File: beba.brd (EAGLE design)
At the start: 35 x 56 mm, 56 parts, among them IC202 LM74670QDGKTQ1, IC302 LM74670QDGKTQ1, IC402 LM74670QDGKTQ1, IC507 579-MCP73871T2CCIML, IC601 TPS630701RNMT, Q202 SQ2310ES-T1_BE3, Q302 SQ2310ES-T1_BE3, Q402 SQ2310ES-T1_BE3

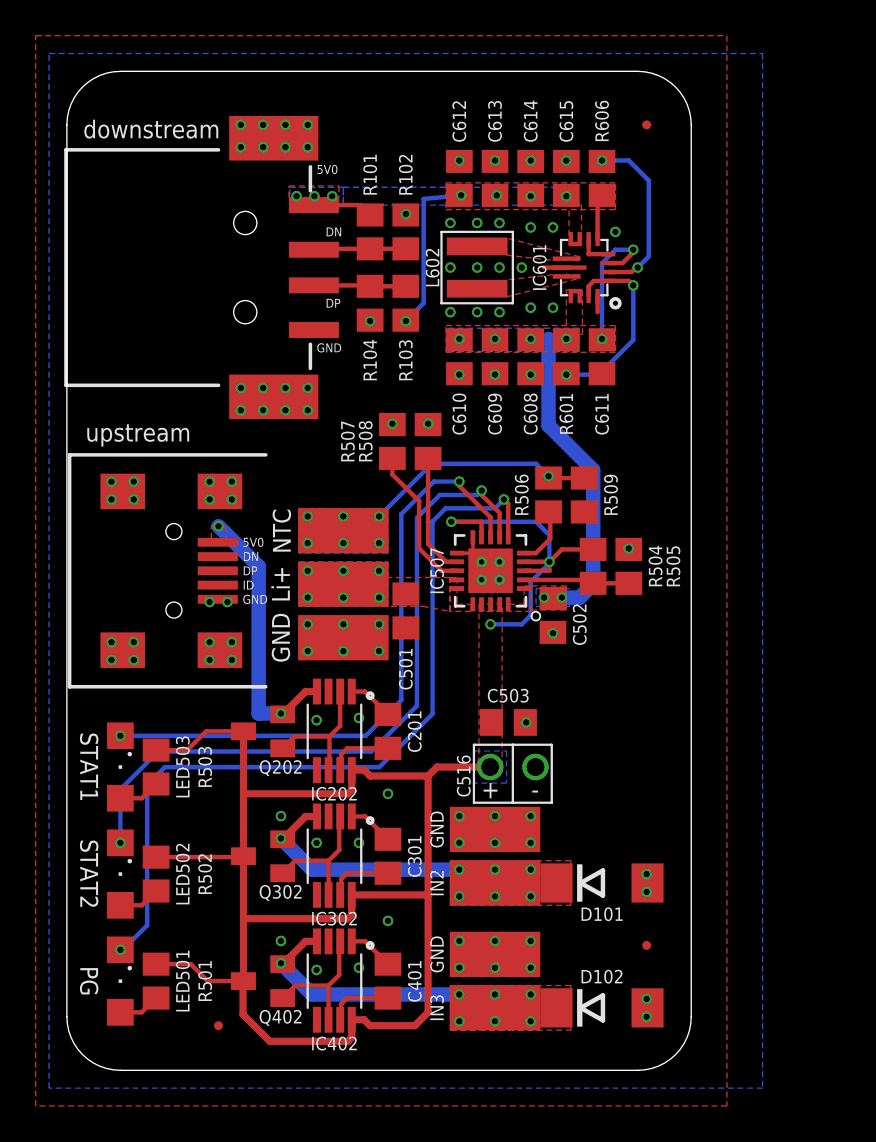
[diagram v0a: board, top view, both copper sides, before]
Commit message: start of rev.2 board - increased uninterrupted copper below MCP73871 for better cooling - removed bottom copper contacts for IN1/IN2, GND and similar - replaced MCP73871's big input cap from TH to SMD - replaced NTC solderpads with 0805 component
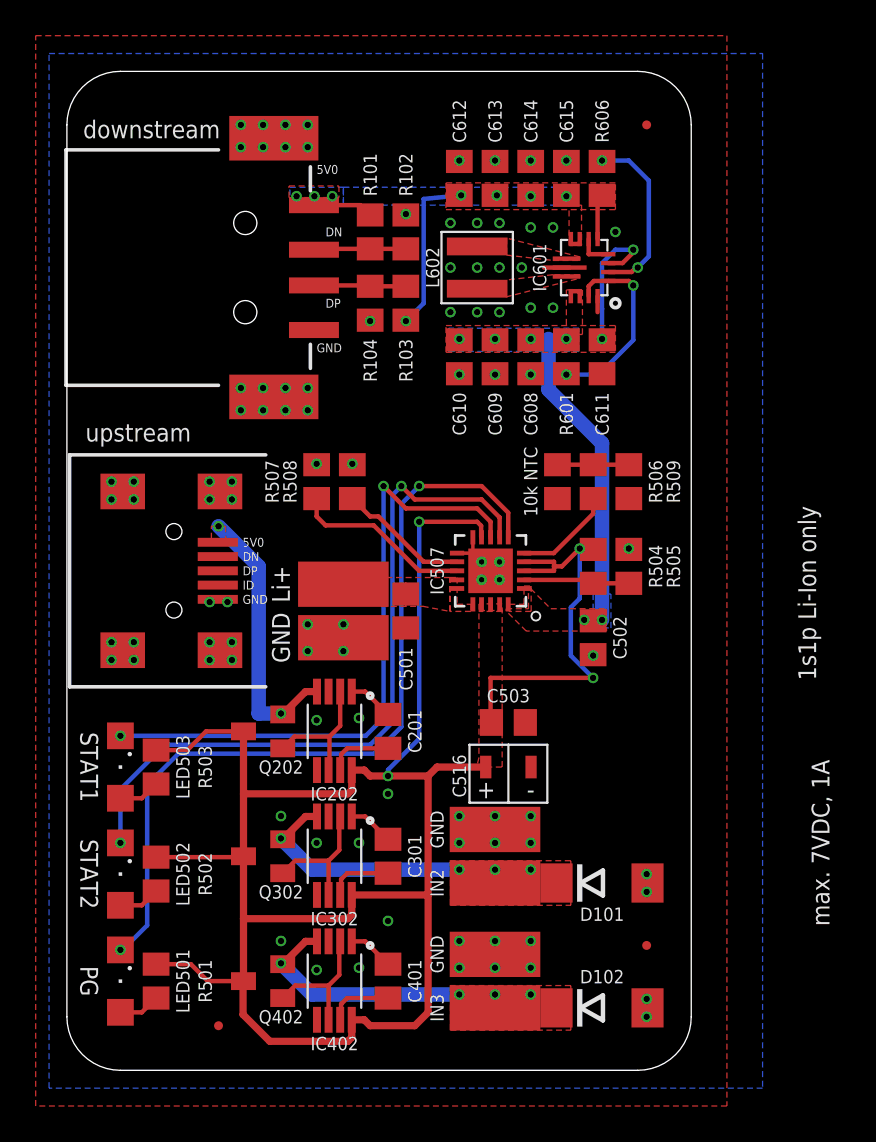
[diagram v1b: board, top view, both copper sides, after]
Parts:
- removed PAD105: NTC, wirepad:SMD2,54-5,08
- added R1: 10k NTC, beta 3892, rcl:R0805
- C516: device C-Pol:TH -> C-Pol:SMD
- moved R507 4.81 mm to (-44.0, 158.0)
- moved R508 4.81 mm to (-42.0, 158.0)
- moved R506 2.61 mm to (-28.5, 158.0)
- moved R509 2.61 mm to (-26.5, 158.0)
- moved C502 2.57 mm to (-28.5, 149.2)
- moved C516 0.25 mm to (-33.2, 142.0)
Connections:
- net GND: now also R1.1
- net NTC: now also R1.2; no longer PAD105.1
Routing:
- net V_INPUT: track 106.0 -> 125.8 mm, vias 3 -> 4
- net NTC: track 13.8 -> 4.00 mm, vias 7 -> 0
- net VINPUT2: track 16.3 -> 20.3 mm, vias 7 -> 4
- net VINPUT3: track 13.3 -> 17.3 mm, vias 7 -> 4
- net MCP73871-1:THERM: track 3.35 -> 5.64 mm
- net MCP73871-1:PROG1: track 8.31 -> 10.1 mm
- net MCP73871-1:PG: track 45.1 -> 46.4 mm
- net MCP73871-1:STAT2: track 39.4 -> 40.6 mm
- net MCP73871-1:STAT1: track 34.9 -> 35.9 mm
- net V_LIION+: track 0.75 -> 0.00 mm, vias 6 -> 0
- net MCP73871-1:PROG3: track 6.83 -> 7.34 mm
- net GND: vias 96 -> 93
- removed copper zone on layer 16, net NTC
- removed copper zone on layer 16, net VINPUT2
- removed copper zone on layer 16, net VINPUT3
- removed copper zone on layer 16, net V_INPUT
- removed copper zone on layer 16, net V_LIION+
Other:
- board text added: "10k NTC"
- board text removed: "NTC"

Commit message: further work on rev.2 board: - increased copper below MCP73871 even more - replaced solder pads for LiIon battery with SMD JST-PH connector
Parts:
- removed FID2: fiducial, fiducials:FIDUCIAL_0.5MM
- removed PAD106: Li-Ion +, wirepad:SMD2,54-5,08
- removed PAD107: GND, wirepad:SMD2,54-5,08
- removed R1: 10k NTC, beta 3892, rcl:R0805
- added FID102: fiducial, fiducials:FIDUCIAL_0.5MM
- added J101: S2B-PH-SM4-TB(LF)(SN), JST-PH:JST_S2B-PH-SM4-TB(LF)(SN)
- added R105: 49k9, resistor:R0805
- added SW701: (no value), JS102011SAQN SPDT slide switch:SMD
- R101: value 75k -> 10k NTC, beta 3892; device resistor:R0805 -> rcl:R0805
- R102, R104: value 49k9 -> 75k
- R103: value 75k -> 49k9
- moved R101 17.5 mm to (-30.5, 158.0)
- moved C611 10.2 mm to (-26.0, 175.0), turned to 270 degrees
- moved R507 6.26 mm to (-41.0, 163.5)
- moved R508 6.26 mm to (-39.0, 163.5)
- moved R103 4.00 mm to (-39.0, 172.0)
- moved R102 2.00 mm to (-41.0, 172.0), turned to 90 degrees
- moved R104 2.00 mm to (-39.0, 168.0), turned to 270 degrees
- moved C501 1.80 mm to (-37.5, 149.8)
- renumbered FID1 to FID101, FID3 to FID103
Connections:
- removed net TPS630701-1:N$8: IC601.1-PS/S, IC601.14-EN, R601.1
- new net TPS630701-1:EN: IC601.14-EN, SW701.C
- new net TPS630701-1:SP/S: IC601.1-PS/S, R601.1, SW701.2
- net 5V0: now also R102.2, R104.2; no longer R101.2, R103.2
- net GND: now also J101.2, J101.S1, J101.S2, R101.1, R103.1, R105.1, SW701.1; no longer PAD107.1, R1.1, R102.1, R104.1
- net NTC: now also R101.2; no longer R1.2
- net USBDN: now also R102.1, R103.2; no longer R101.1, R102.2
- net USBDP: now also R104.1, R105.2; no longer R103.1, R104.2
- net V_LIION+: now also J101.1; no longer PAD106.1
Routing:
- net TPS630701-1:SP/S: track 0.00 -> 35.1 mm, vias 0 -> 2
- net TPS630701-1:EN: track 0.00 -> 31.9 mm
- net 5V0: track 16.0 -> 36.5 mm, vias 8 -> 7
- net TPS630701-1:N$8: track 11.0 -> 0.00 mm, vias 2 -> 0
- net MCP73871-1:STAT2: track 40.6 -> 45.6 mm
- net MCP73871-1:PROG3: track 7.34 -> 12.2 mm
- net MCP73871-1:PG: track 46.4 -> 50.5 mm
- net MCP73871-1:STAT1: track 35.9 -> 39.6 mm
- net TPS630701-1:VAUX: track 8.16 -> 5.01 mm, vias 2 -> 0
- net V_REGULATED: track 18.0 -> 21.0 mm
- net MCP73871-1:PROG1: track 10.1 -> 12.7 mm
- net V_INPUT: track 125.8 -> 127.3 mm
- net TPS630701-1:PG1: track 10.0 -> 8.78 mm
- net GND: track 6.06 -> 7.27 mm, vias 93 -> 107
- added copper zone on layer 16, net V_LIION+
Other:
- board text added: "5V0 out"
- board text added: "Input1"
- board text added: "Input2"
- board text added: "Input3"
- board text added: "OFF"
- board text added: "ON"
- board text added: "USB out"
- board text added: "Vreg"
- board text added: "beba rev.2"
- board text removed: "beba rev.1"

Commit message: more work
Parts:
- SW701: value (none) -> JS102011SAQN
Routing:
- net MCP73871-1:PROG3: track 12.2 -> 10.7 mm
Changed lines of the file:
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@@
 <attribute name="VALUE" x="-27.96" y="157.365" size="1.27" layer="27" rot="R90"/>
 </element>
-<element name="SW701" library="JS102011SAQN SPDT slide switch" package="SMD" value="" x="-29.5" y="142" smashed="yes" rot="R90">
+<element name="SW701" library="JS102011SAQN SPDT slide switch" package="SMD" value="JS102011SAQN" x="-29.5" y="142" smashed="yes" rot="R90">
 <attribute name="NAME" x="-26.75" y="142" size="0.75" layer="25" rot="R270" align="center"/>
 <attribute name="VALUE" x="-26.96" y="147.08" size="0.75" layer="27" rot="R180" align="center"/>
@@
 <contactref element="IC507" pad="7_STAT2"/>
 <via x="-55" y="137.75" extent="1-16" drill="0.35"/>
-<via x="-38.75" y="160.25" extent="1-16" drill="0.35"/>
+<via x="-36.5" y="160.25" extent="1-16" drill="0.35"/>
 <wire x1="-33.742" y1="154.8796" x2="-33.742" y2="155.992" width="0.25" layer="1"/>
 <wire x1="-33.742" y1="155.992" x2="-36.5" y2="158.75" width="0.25" layer="1"/>
-<wire x1="-36.5" y1="158.75" x2="-38.25" y2="158.75" width="0.25" layer="1"/>
-<wire x1="-38.25" y1="158.75" x2="-38.75" y2="159.25" width="0.25" layer="1"/>
-<wire x1="-38.75" y1="159.25" x2="-38.75" y2="160.25" width="0.25" layer="1"/>
+<wire x1="-36.5" y1="158.75" x2="-36.5" y2="160.25" width="0.25" layer="1"/>
 <wire x1="-53" y1="138.25" x2="-53.5" y2="137.75" width="0.25" layer="16"/>
 <wire x1="-55" y1="137.75" x2="-53.5" y2="137.75" width="0.25" layer="16"/>
@@
 <wire x1="-53" y1="156.5" x2="-53" y2="157.25" width="0.25" layer="16"/>
 <wire x1="-53" y1="157.25" x2="-50" y2="160.25" width="0.25" layer="16"/>
-<wire x1="-50" y1="160.25" x2="-38.75" y2="160.25" width="0.25" layer="16"/>
+<wire x1="-50" y1="160.25" x2="-36.5" y2="160.25" width="0.25" layer="16"/>
 </signal>
 <signal name="MCP73871-1:STAT1" class="2">
@@
 <contactref element="IC507" pad="8_STAT1/!LBO!"/>
 <via x="-55" y="143.75" extent="1-16" drill="0.35"/>
-<via x="-39.5" y="161" extent="1-16" drill="0.35"/>
+<via x="-37.25" y="161" extent="1-16" drill="0.35"/>
 <wire x1="-34.25" y1="155.75" x2="-34.25" y2="154.8796" width="0.25" layer="1"/>
-<wire x1="-39.5" y1="161" x2="-50" y2="161" width="0.25" layer="16"/>
+<wire x1="-37.25" y1="161" x2="-50" y2="161" width="0.25" layer="16"/>
 <wire x1="-53.5" y1="156.75" x2="-54" y2="156.25" width="0.25" layer="16"/>
 <wire x1="-50" y1="161" x2="-53.5" y2="157.5" width="0.25" layer="16"/>
@@
 <wire x1="-53.5" y1="145.25" x2="-55" y2="143.75" width="0.25" layer="16"/>
 <wire x1="-54" y1="156.25" x2="-54" y2="149.75" width="0.25" layer="16"/>
-<wire x1="-39.5" y1="161" x2="-39.5" y2="159.25" width="0.25" layer="1"/>
-<wire x1="-38.377" y1="158.127" x2="-36.627" y2="158.127" width="0.25" layer="1"/>
-<wire x1="-39.5" y1="159.25" x2="-38.377" y2="158.127" width="0.25" layer="1"/>
-<wire x1="-36.627" y1="158.127" x2="-34.25" y2="155.75" width="0.25" layer="1"/>
+<wire x1="-37.25" y1="161" x2="-37.25" y2="158.75" width="0.25" layer="1"/>
+<wire x1="-37.25" y1="158.75" x2="-34.25" y2="155.75" width="0.25" layer="1"/>
 </signal>
 <signal name="MCP73871-1:PG" class="2">
@@
 <contactref element="IC507" pad="!6_PG!"/>
 <via x="-55" y="131.75" extent="1-16" drill="0.35"/>
-<via x="-38" y="159.5" extent="1-16" drill="0.35"/>
+<via x="-35.75" y="159.5" extent="1-16" drill="0.35"/>
 <wire x1="-33.2594" y1="154.8796" x2="-33.2594" y2="156.2594" width="0.25" layer="1"/>
-<wire x1="-33.2594" y1="156.2594" x2="-36.5" y2="159.5" width="0.25" layer="1"/>
-<wire x1="-36.5" y1="159.5" x2="-38" y2="159.5" width="0.25" layer="1"/>
+<wire x1="-33.2594" y1="156.2594" x2="-35.75" y2="158.75" width="0.25" layer="1"/>
+<wire x1="-35.75" y1="158.75" x2="-35.75" y2="159.5" width="0.25" layer="1"/>
 <wire x1="-53.625" y1="131.75" x2="-55" y2="131.75" width="0.25" layer="16"/>
-<wire x1="-38" y1="159.5" x2="-50" y2="159.5" width="0.25" layer="16"/>
+<wire x1="-35.75" y1="159.5" x2="-50" y2="159.5" width="0.25" layer="16"/>
 <wire x1="-53" y1="155.75" x2="-53" y2="150.25" width="0.25" layer="16"/>
 <wire x1="-53" y1="150.25" x2="-52.5" y2="149.75" width="0.25" layer="16"/>
@@
 <contactref element="R508" pad="1"/>
 <contactref element="IC507" pad="12_PROG3"/>
-<wire x1="-39" y1="162.55" x2="-39.00961875" y2="162.55" width="0.25" layer="1"/>
-<wire x1="-40.225" y1="161.33461875" x2="-39.00961875" y2="162.55" width="0.25" layer="1"/>
 <wire x1="-37" y1="153.508" x2="-36.1296" y2="153.508" width="0.25" layer="1"/>
-<wire x1="-40.225" y1="159.225" x2="-38.5" y2="157.5" width="0.25" layer="1"/>
-<wire x1="-40.225" y1="159.225" x2="-40.225" y2="161.33461875" width="0.25" layer="1"/>
-<wire x1="-38.5" y1="157.5" x2="-37.75" y2="157.5" width="0.25" layer="1"/>
-<wire x1="-37.75" y1="157.5" x2="-37" y2="156.75" width="0.25" layer="1"/>
+<wire x1="-38.975" y1="158.725" x2="-37" y2="156.75" width="0.25" layer="1"/>
+<wire x1="-39" y1="162.55" x2="-38.975" y2="162.525" width="0.25" layer="1"/>
+<wire x1="-38.975" y1="162.525" x2="-38.975" y2="158.725" width="0.25" layer="1"/>
 <wire x1="-37" y1="156.75" x2="-37" y2="153.508" width="0.25" layer="1"/>
 </signal>
@@
 <wire x1="-36.1296" y1="153" x2="-37.25" y2="153" width="0.25" layer="1"/>
 <wire x1="-37.25" y1="153" x2="-37.75" y2="153.5" width="0.25" layer="1"/>
-<wire x1="-37.75" y1="156.75" x2="-38.025" y2="157.025" width="0.25" layer="1"/>
-<wire x1="-38.025" y1="157.025" x2="-38.775" y2="157.025" width="0.25" layer="1"/>
-<wire x1="-38.775" y1="157.025" x2="-41" y2="159.25" width="0.25" layer="1"/>
+<wire x1="-37.75" y1="156.75" x2="-41" y2="160" width="0.25" layer="1"/>
 <wire x1="-37.75" y1="153.5" x2="-37.75" y2="156.75" width="0.25" layer="1"/>
-<wire x1="-41" y1="159.25" x2="-41" y2="162.55" width="0.25" layer="1"/>
+<wire x1="-41" y1="160" x2="-41" y2="162.55" width="0.25" layer="1"/>
 </signal>
 <signal name="TPS630701-1:SP/S" class="2">
